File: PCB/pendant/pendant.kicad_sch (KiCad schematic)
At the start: 9 parts, among them J1 Conn_02x10_Odd_Even, J2 Conn_01x12, J3 Conn_01x03, J4 Conn_01x02, Q1 2N3904, Q2 2N3904, U1 Pico

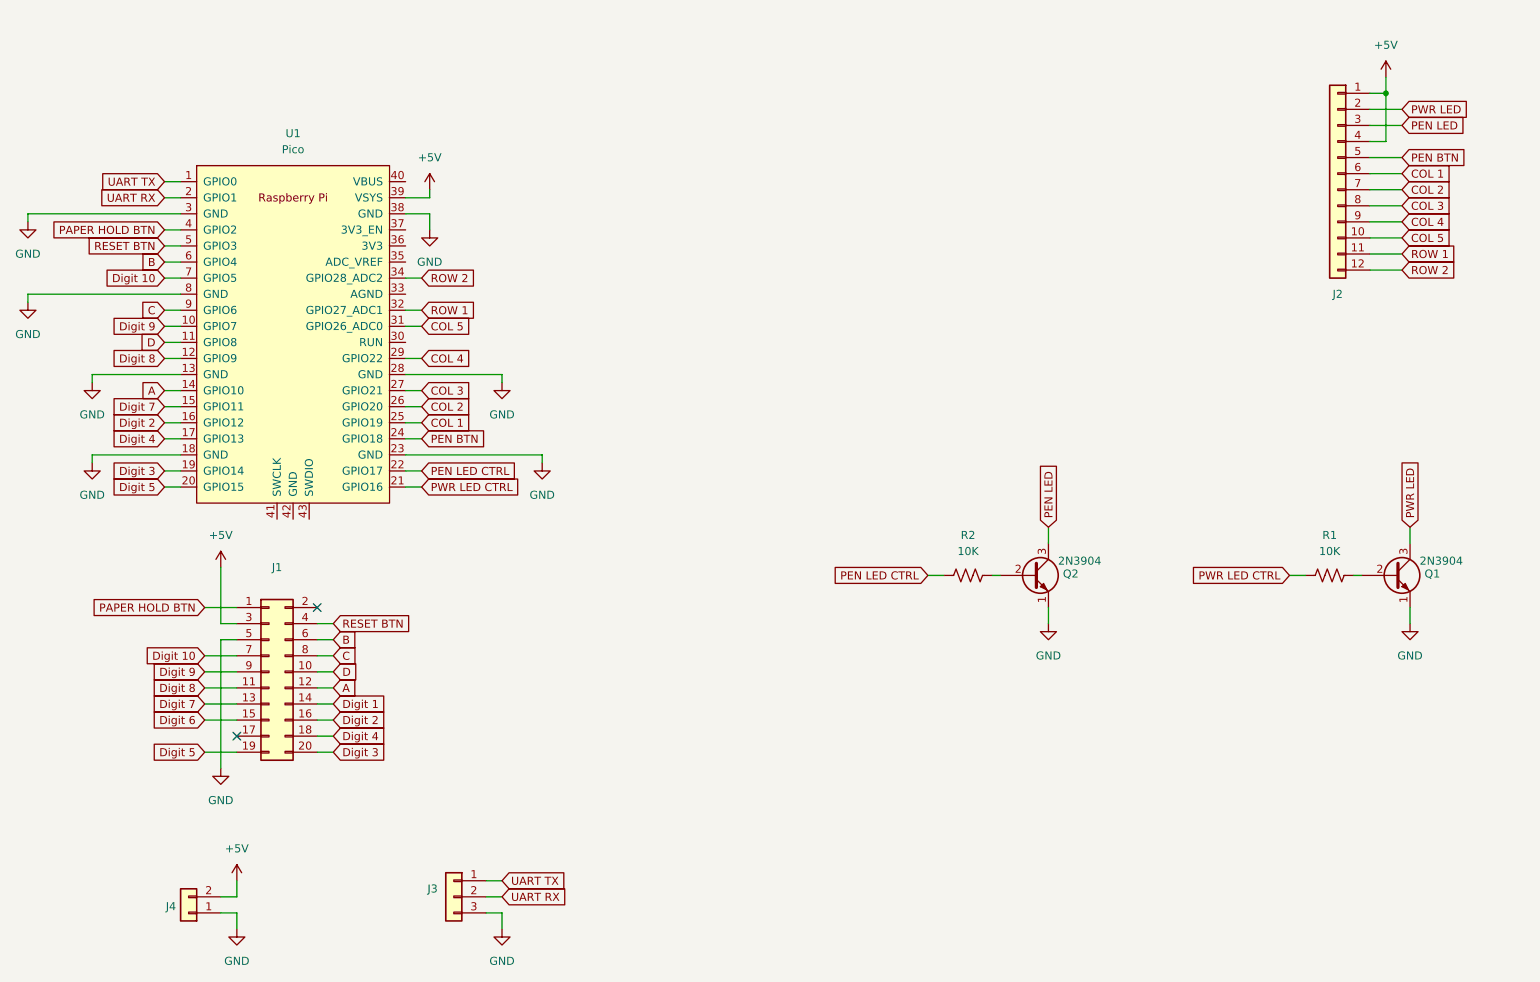
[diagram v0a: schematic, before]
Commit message: feat: Redesign Pendant circuit and add stepper control circuit
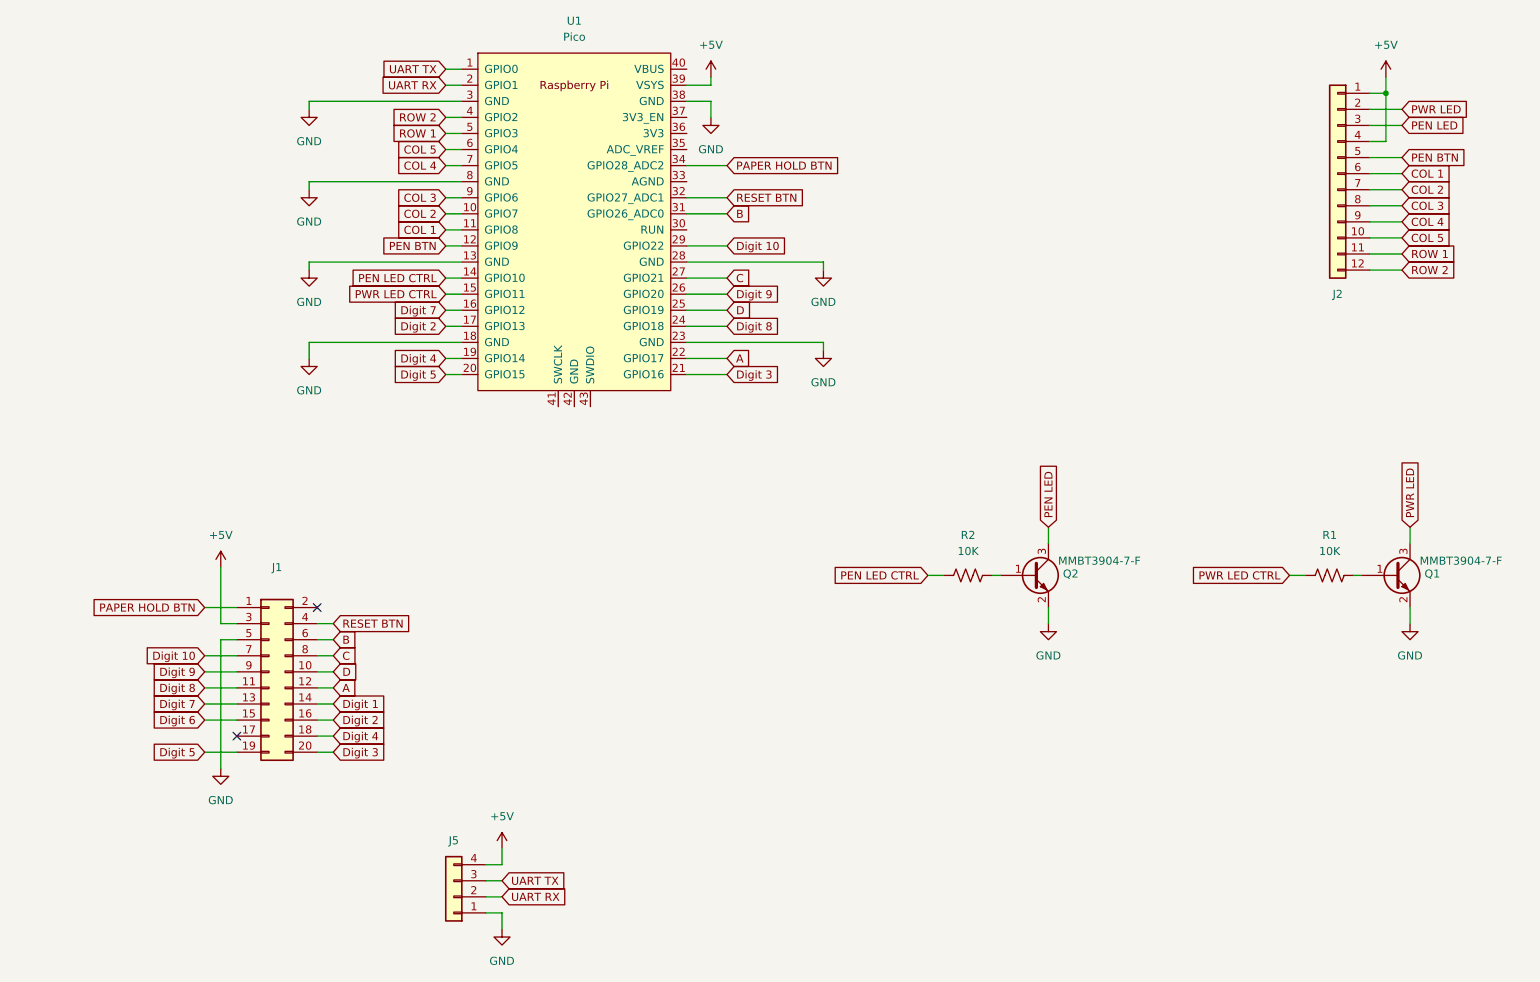
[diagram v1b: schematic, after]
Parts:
- removed J3: Conn_01x03, Connector_PinHeader_2.54mm:PinHeader_1x03_P2.54mm_Vertical, symbol Connector_Generic:Conn_01x03
- removed J4: Conn_01x02, Connector_PinHeader_2.54mm:PinHeader_1x02_P2.54mm_Vertical, symbol Connector_Generic:Conn_01x02
- added J5: Conn_01x04, Connector_PinHeader_2.54mm:PinHeader_1x04_P2.54mm_Vertical, symbol Connector_Generic:Conn_01x04
- J1: footprint Connector_IDC:IDC-Header_2x10_P2.54mm_Vertical -> Connector_PinHeader_1.27mm:PinHeader_1x20_P1.27mm_Vertical
- J2: footprint Connector_PinHeader_2.00mm:PinHeader_1x12_P2.00mm_Vertical -> Connector_PinHeader_2.54mm:PinHeader_1x12_P2.54mm_Vertical
- Q1, Q2: value 2N3904 -> MMBT3904-7-F; footprint Package_TO_SOT_THT:TO-92_Inline -> Package_TO_SOT_SMD:SOT-23
- R1, R2: footprint Resistor_THT:R_Axial_DIN0207_L6.3mm_D2.5mm_P10.16mm_Horizontal -> Resistor_SMD:R_0603_1608Metric
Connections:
- net +5V: now also J5.4 (Pin_4)
- net A: now also U1.22 (GPIO17); no longer U1.14 (GPIO10)
- net B: now also U1.31 (GPIO26_ADC0); no longer U1.6 (GPIO4)
- net C: now also U1.27 (GPIO21); no longer U1.9 (GPIO6)
- net COL 1: now also U1.11 (GPIO8); no longer U1.25 (GPIO19)
- net COL 2: now also U1.10 (GPIO7); no longer U1.26 (GPIO20)
- net COL 3: now also U1.9 (GPIO6); no longer U1.27 (GPIO21)
- net COL 4: now also U1.7 (GPIO5); no longer U1.29 (GPIO22)
- net COL 5: now also U1.6 (GPIO4); no longer U1.31 (GPIO26_ADC0)
- net D: now also U1.25 (GPIO19); no longer U1.11 (GPIO8)
- net Digit 10: now also U1.29 (GPIO22); no longer U1.7 (GPIO5)
- net Digit 2: now also U1.17 (GPIO13); no longer U1.16 (GPIO12)
- net Digit 3: now also U1.21 (GPIO16); no longer U1.19 (GPIO14)
- net Digit 4: now also U1.19 (GPIO14); no longer U1.17 (GPIO13)
- net Digit 7: now also U1.16 (GPIO12); no longer U1.15 (GPIO11)
- net Digit 8: now also U1.24 (GPIO18); no longer U1.12 (GPIO9)
- net Digit 9: now also U1.26 (GPIO20); no longer U1.10 (GPIO7)
- net GND: now also Q1.2 (E), Q2.2 (E), J5.1 (Pin_1); no longer Q1.1 (E), Q2.1 (E)
- net PAPER HOLD BTN: now also U1.34 (GPIO28_ADC2); no longer U1.4 (GPIO2)
- net PEN BTN: now also U1.12 (GPIO9); no longer U1.24 (GPIO18)
- net PEN LED CTRL: now also U1.14 (GPIO10); no longer U1.22 (GPIO17)
- net PWR LED CTRL: now also U1.15 (GPIO11); no longer U1.21 (GPIO16)
- net RESET BTN: now also U1.32 (GPIO27_ADC1); no longer U1.5 (GPIO3)
- net ROW 1: now also U1.5 (GPIO3); no longer U1.32 (GPIO27_ADC1)
- net ROW 2: now also U1.4 (GPIO2); no longer U1.34 (GPIO28_ADC2)
- net UART RX: now also J5.2 (Pin_2)
- net UART TX: now also J5.3 (Pin_3)
- net at R1.2: now also Q1.1 (B); no longer Q1.2 (B)
- net at R2.2: now also Q2.1 (B); no longer Q2.2 (B)
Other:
- moved on the sheet: U1
